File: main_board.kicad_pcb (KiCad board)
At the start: 2 copper layers, 142.2 x 86.4 mm, 4 parts, among them P1 CONN_02X04, U1 socket_leon_x3_dil64, U2 socket_pololu_24v12, U3 socket_pololu_24v12

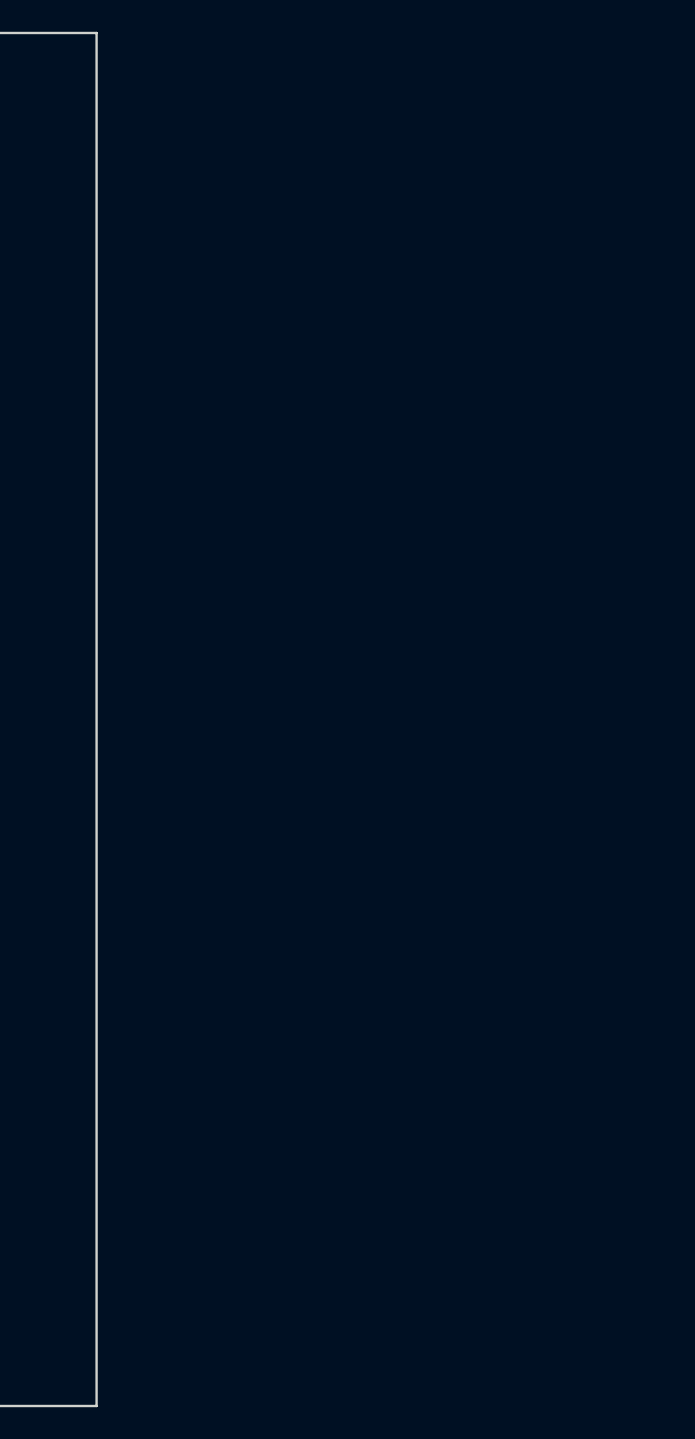
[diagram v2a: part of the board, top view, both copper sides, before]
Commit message: pcb: fix width size
Signed-off-by: Yannick Gicquel <ygicquel@gmail.com>
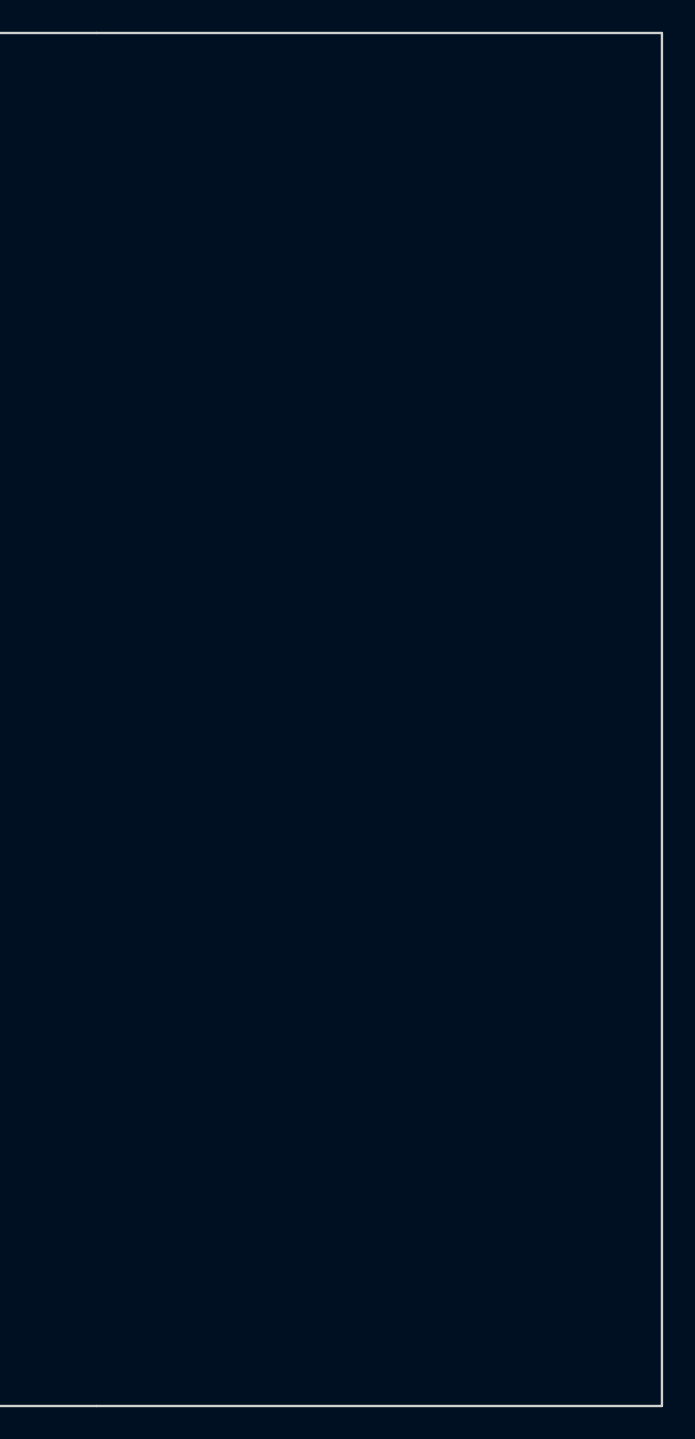
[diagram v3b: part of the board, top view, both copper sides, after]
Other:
- board size 142.2 x 86.4 mm -> 177.8 x 86.4 mm
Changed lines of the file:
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@@
     (links 27)
     (no_connects 25)
-    (area 35.484999 49.454999 177.875001 135.965001)
+    (area 35.484999 49.254999 177.875001 135.965001)
     (thickness 1.6)
-    (drawings 4)
+    (drawings 6)
     (tracks 6)
     (zones 0)
@@
     )
   )
-  (gr_line (start 177.8 49.53) (end 177.8 135.89) (angle 90) (layer Edge.Cuts) (width 0.15))
+  (gr_line (start 213.36 49.53) (end 177.8 49.53) (angle 90) (layer Edge.Cuts) (width 0.15))
+  (gr_line (start 213.36 135.89) (end 213.36 49.53) (angle 90) (layer Edge.Cuts) (width 0.15))
+  (gr_line (start 177.8 135.89) (end 213.36 135.89) (angle 90) (layer Edge.Cuts) (width 0.15))
   (gr_line (start 35.56 135.89) (end 35.56 49.53) (angle 90) (layer Edge.Cuts) (width 0.15))
   (gr_line (start 177.8 49.53) (end 35.56 49.53) (angle 90) (layer Edge.Cuts) (width 0.15))

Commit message: pcb: routing test and holes
Signed-off-by: Yannick Gicquel <ygicquel@gmail.com>
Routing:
- net ENC_B_L: track 0.00 -> 93.9 mm
- net PWM_R: track 0.00 -> 92.0 mm
- net ENC_A_L: track 0.00 -> 51.1 mm
- net DIR_L: track 0.00 -> 47.3 mm
- net DIR_R: track 0.00 -> 28.8 mm
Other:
- outline, holes or cut-outs redrawn
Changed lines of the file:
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@@
   (general
     (links 27)
-    (no_connects 25)
+    (no_connects 20)
     (area 35.484999 49.254999 177.875001 135.965001)
     (thickness 1.6)
-    (drawings 6)
-    (tracks 6)
+    (drawings 10)
+    (tracks 37)
     (zones 0)
     (modules 4)
@@
     )
   )
+  (gr_circle (center 39.37 53.34) (end 40.64 53.34) (layer Edge.Cuts) (width 0.15))
+  (gr_circle (center 209.55 53.34) (end 209.55 52.07) (layer Edge.Cuts) (width 0.15))
+  (gr_circle (center 209.55 132.08) (end 210.82 132.08) (layer Edge.Cuts) (width 0.15))
+  (gr_circle (center 39.37 132.08) (end 40.64 132.08) (layer Edge.Cuts) (width 0.15))
   (gr_line (start 213.36 49.53) (end 177.8 49.53) (angle 90) (layer Edge.Cuts) (width 0.15))
   (gr_line (start 213.36 135.89) (end 213.36 49.53) (angle 90) (layer Edge.Cuts) (width 0.15))
@@
   (gr_line (start 177.8 49.53) (end 35.56 49.53) (angle 90) (layer Edge.Cuts) (width 0.15))
   (gr_line (start 35.56 135.89) (end 177.8 135.89) (angle 90) (layer Edge.Cuts) (width 0.15))
+  (segment (start 74.93 105.41) (end 74.93 69.85) (width 0.25) (layer B.Cu) (net 63))
+  (segment (start 78.74 66.04) (end 85.09 66.04) (width 0.25) (layer B.Cu) (net 63))
+  (segment (start 74.93 69.85) (end 78.74 66.04) (width 0.25) (layer B.Cu) (net 63))
+  (segment (start 72.39 105.41) (end 72.39 106.68) (width 0.25) (layer B.Cu) (net 64))
+  (segment (start 78.74 91.44) (end 85.09 91.44) (width 0.25) (layer B.Cu) (net 64))
+  (segment (start 76.2 93.98) (end 78.74 91.44) (width 0.25) (layer B.Cu) (net 64))
+  (segment (start 76.2 106.68) (end 76.2 93.98) (width 0.25) (layer B.Cu) (net 64))
+  (segment (start 74.93 107.95) (end 76.2 106.68) (width 0.25) (layer B.Cu) (net 64))
+  (segment (start 73.66 107.95) (end 74.93 107.95) (width 0.25) (layer B.Cu) (net 64))
+  (segment (start 72.39 106.68) (end 73.66 107.95) (width 0.25) (layer B.Cu) (net 64))
+  (segment (start 77.47 128.27) (end 77.47 128.62) (width 0.25) (layer B.Cu) (net 65))
+  (segment (start 104.14 88.9) (end 85.09 88.9) (width 0.25) (layer B.Cu) (net 66))
+  (segment (start 106.68 91.44) (end 104.14 88.9) (width 0.25) (layer B.Cu) (net 66))
+  (segment (start 106.68 130.81) (end 106.68 91.44) (width 0.25) (layer B.Cu) (net 66))
+  (segment (start 84.74 133.35) (end 104.14 133.35) (width 0.25) (layer B.Cu) (net 66))
+  (segment (start 104.14 133.35) (end 106.68 130.81) (width 0.25) (layer B.Cu) (net 66))
+  (segment (start 80.01 128.27) (end 80.01 128.62) (width 0.25) (layer B.Cu) (net 66))
+  (segment (start 80.01 128.62) (end 84.74 133.35) (width 0.25) (layer B.Cu) (net 66))
+  (segment (start 43.18 116.84) (end 44.45 118.11) (width 0.25) (layer B.Cu) (net 67))
+  (segment (start 85.09 120.65) (end 85.09 128.27) (width 0.25) (layer B.Cu) (net 67))
+  (segment (start 82.55 118.11) (end 85.09 120.65) (width 0.25) (layer B.Cu) (net 67))
+  (segment (start 44.45 118.11) (end 82.55 118.11) (width 0.25) (layer B.Cu) (net 67))
+  (segment (start 104.14 121.92) (end 104.14 130.81) (width 0.25) (layer B.Cu) (net 68))
+  (segment (start 44.45 115.57) (end 99.06 115.57) (width 0.25) (layer B.Cu) (net 68))
+  (segment (start 99.06 115.57) (end 104.14 120.65) (width 0.25) (layer B.Cu) (net 68))
+  (segment (start 104.14 120.65) (end 104.14 121.92) (width 0.25) (layer B.Cu) (net 68))
+  (segment (start 43.18 114.3) (end 44.45 115.57) (width 0.25) (layer B.Cu) (net 68))
+  (segment (start 87.63 130.81) (end 87.63 128.27) (width 0.25) (layer B.Cu) (net 68))
+  (segment (start 88.9 132.08) (end 87.63 130.81) (width 0.25) (layer B.Cu) (net 68))
+  (segment (start 102.87 132.08) (end 88.9 132.08) (width 0.25) (layer B.Cu) (net 68))
+  (segment (start 104.14 130.81) (end 102.87 132.08) (width 0.25) (layer B.Cu) (net 68))
   (segment (start 102.87 128.27) (end 102.87 120.65) (width 0.25) (layer B.Cu) (net 69))
   (segment (start 99.06 116.84) (end 45.72 116.84) (width 0.25) (layer B.Cu) (net 69))

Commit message: all: add UARTC0 (debug link)
Signed-off-by: Yannick Gicquel <ygicquel@gmail.com>
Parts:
- added P2: CONN_01X05, Pin_Headers:Pin_Header_Straight_1x05, F.Cu at (128.3, 55.9)
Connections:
- U1 pad 18: Net-(U1-Pad18) -> UART0_TXD
- U1 pad 19: Net-(U1-Pad19) -> UART0_RXD

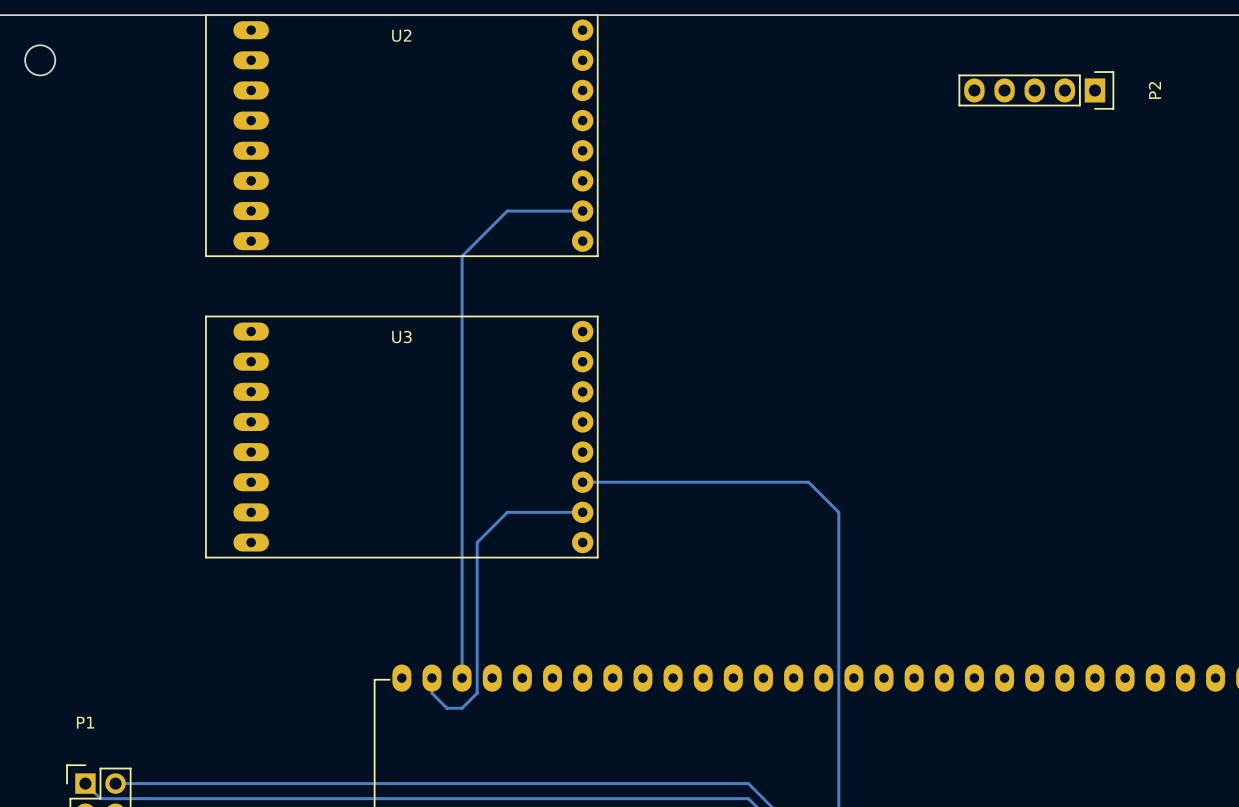
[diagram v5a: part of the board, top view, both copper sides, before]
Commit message: sch: move to hierarchical schematic and multiple sheets
Signed-off-by: Yannick Gicquel <ygicquel@gmail.com>
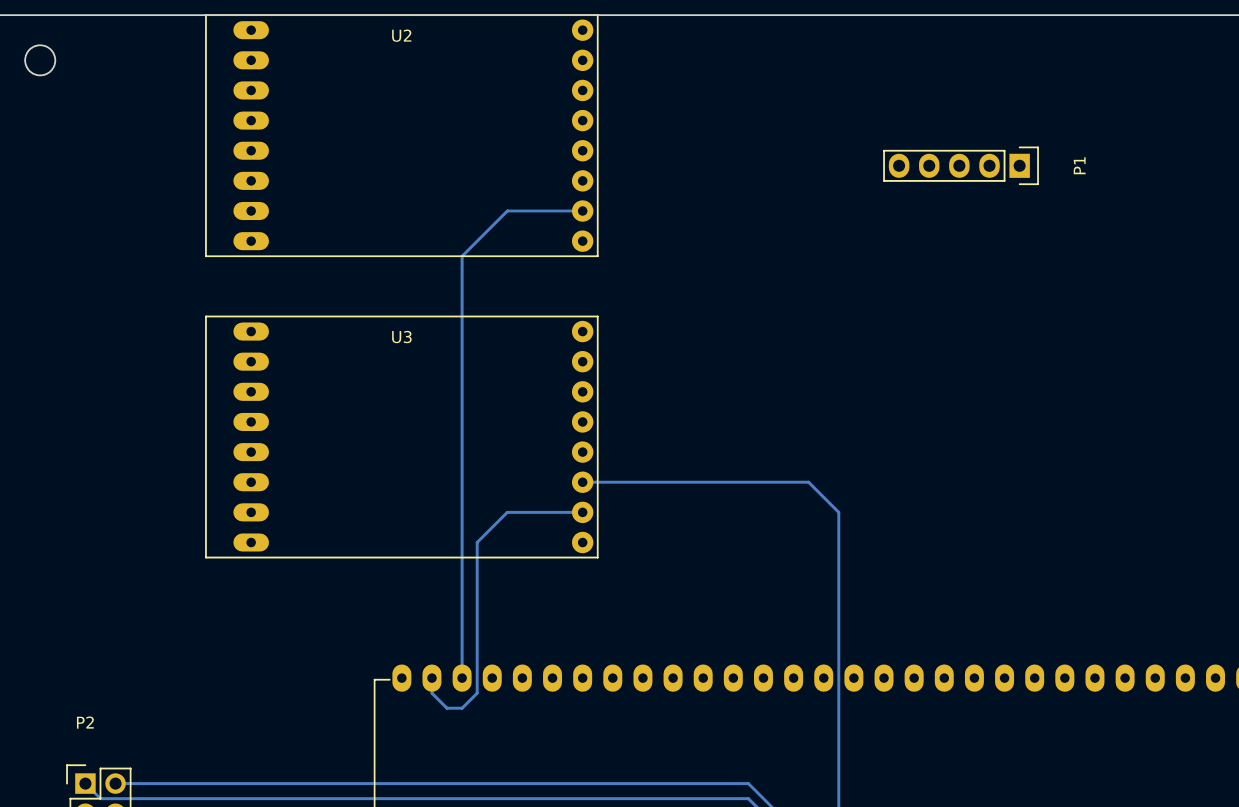
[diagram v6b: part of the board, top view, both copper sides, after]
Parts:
- P1: value CONN_02X04 -> CONN_01X05; footprint Pin_Headers:Pin_Header_Straight_2x04 -> Pin_Headers:Pin_Header_Straight_1x05
- P2: value CONN_01X05 -> CONN_02X04; footprint Pin_Headers:Pin_Header_Straight_1x05 -> Pin_Headers:Pin_Header_Straight_2x04
- moved P2 103.2 mm to (43.2, 114.3), turned to 0 degrees
- moved P1 94.4 mm to (121.9, 62.2), turned to 270 degrees
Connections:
- net DIR_L renamed /Sheet_MCU/DIR_L
- net DIR_R renamed /Sheet_MCU/DIR_R
- net OUTA_L renamed /Sheet_Motors/OUTA_L
- net OUTA_R renamed /Sheet_Motors/OUTA_R
- net OUTB_L renamed /Sheet_Motors/OUTB_L
- net OUTB_R renamed /Sheet_Motors/OUTB_R
- net PWM_L renamed /Sheet_MCU/PWM_L
- net PWM_R renamed /Sheet_MCU/PWM_R
- P1 pad 1: ENC_B_L -> Net-(P1-Pad1)
- P1 pad 2: ENC_B_R -> /Sheet_Connectors/UART_DBG_TXD
- P1 pad 3: ENC_A_L -> /Sheet_Connectors/UART_DBG_RXD
- P1 pad 4: ENC_A_R -> GND
- P1 pad 5: +3V3 -> Net-(P1-Pad5)
- P2 pad 1: Net-(P2-Pad1) -> ENCB_L
- P2 pad 2: UART0_TXD -> ENCB_R
- P2 pad 3: UART0_RXD -> ENCA_L
- P2 pad 4: GND -> ENCA_R
- P2 pad 5: Net-(P2-Pad5) -> +3V3
- U1 pad 18: UART0_TXD -> /Sheet_Connectors/UART_DBG_TXD
- U1 pad 19: UART0_RXD -> /Sheet_Connectors/UART_DBG_RXD
- U1 pad 39: ENC_A_L -> ENCA_L
- U1 pad 40: ENC_B_L -> ENCB_L
- U1 pad 46: ENC_A_R -> ENCA_R
- U1 pad 47: ENC_B_R -> ENCB_R
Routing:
- net ENC_B_L: track 93.9 -> 0.00 mm
- net ENCB_L: track 0.00 -> 93.9 mm
- net ENC_B_R: track 69.9 -> 0.00 mm
- net ENCB_R: track 0.00 -> 69.9 mm
- net ENC_A_R: track 66.3 -> 0.00 mm
- net ENCA_R: track 0.00 -> 66.3 mm
- net ENC_A_L: track 51.1 -> 0.00 mm
- net ENCA_L: track 0.00 -> 51.1 mm

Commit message: sch: add main_board_psu
subsheet contains PSU relevant parts

Signed-off-by: Yannick Gicquel <ygicquel@gmail.com>
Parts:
- added P3: CONN_01X02, Terminal_Blocks:TerminalBlock_Pheonix_MKDS1.5-2pol, F.Cu at (191.8, 57.1)
- added U4: socket_lm2596_mod, bot_parts:lm2596s_mod, F.Cu at (157.5, 68.6)
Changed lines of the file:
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@@
-(kicad_pcb (version 4) (host pcbnew 4.0.2+e4-6225~38~ubuntu15.10.1-stable)
+(kicad_pcb (version 4) (host pcbnew 4.0.4+e1-6308~48~ubuntu16.04.1-stable)
   (general
-    (links 30)
-    (no_connects 23)
+    (links 35)
+    (no_connects 28)
     (area 35.484999 49.454999 213.435001 135.965001)
     (thickness 1.6)
@@
     (tracks 37)
     (zones 0)
-    (modules 5)
-    (nets 80)
+    (modules 7)
+    (nets 81)
   )
   (page A4)
@@
   (net 78 /Sheet_Motors/OUTA_R)
   (net 79 /Sheet_Motors/OUTB_R)
+  (net 80 +5V)
   (net_class Default "This is the default net class."
     (clearance 0.2)
@@
     (add_net +24V)
     (add_net +3V3)
+    (add_net +5V)
     (add_net /Sheet_Connectors/UART_DBG_RXD)
     (add_net /Sheet_Connectors/UART_DBG_TXD)
@@
     )
   )
+  (module Terminal_Blocks:TerminalBlock_Pheonix_MKDS1.5-2pol (layer F.Cu)
+    (at 191.77 57.15)
+    (descr "2-way 5mm pitch terminal block, Phoenix MKDS series")
+    (fp_text reference P3 (at 2.5 5.9) (layer F.SilkS)
+      (effects (font (size 1 1) (thickness 0.15)))
+    )
+    (fp_text value CONN_01X02 (at 2.5 -6.6) (layer F.Fab)
+      (effects (font (size 1 1) (thickness 0.15)))
+    )
+    (fp_line (start -2.7 -5.4) (end 7.7 -5.4) (layer F.CrtYd) (width 0.05))
+    (fp_line (start -2.7 4.8) (end -2.7 -5.4) (layer F.CrtYd) (width 0.05))
+    (fp_line (start 7.7 4.8) (end -2.7 4.8) (layer F.CrtYd) (width 0.05))
+    (fp_line (start 7.7 -5.4) (end 7.7 4.8) (layer F.CrtYd) (width 0.05))
+    (fp_line (start 2.5 4.1) (end 2.5 4.6) (layer F.SilkS) (width 0.15))
+    (fp_circle (center 5 0.1) (end 3 0.1) (layer F.SilkS) (width 0.15))
+    (fp_circle (center 0 0.1) (end 2 0.1) (layer F.SilkS) (width 0.15))
+    (fp_line (start -2.5 2.6) (end 7.5 2.6) (layer F.SilkS) (width 0.15))
+    (fp_line (start -2.5 -2.3) (end 7.5 -2.3) (layer F.SilkS) (width 0.15))
+    (fp_line (start -2.5 4.1) (end 7.5 4.1) (layer F.SilkS) (width 0.15))
+    (fp_line (start -2.5 4.6) (end 7.5 4.6) (layer F.SilkS) (width 0.15))
+    (fp_line (start 7.5 4.6) (end 7.5 -5.2) (layer F.SilkS) (width 0.15))
+    (fp_line (start 7.5 -5.2) (end -2.5 -5.2) (layer F.SilkS) (width 0.15))
+    (fp_line (start -2.5 -5.2) (end -2.5 4.6) (layer F.SilkS) (width 0.15))
+    (pad 1 thru_hole rect (at 0 0) (size 2.5 2.5) (drill 1.3) (layers *.Cu *.Mask F.SilkS)
+      (net 62 GND))
+    (pad 2 thru_hole circle (at 5 0) (size 2.5 2.5) (drill 1.3) (layers *.Cu *.Mask F.SilkS)
+      (net 61 +24V))
+    (model Terminal_Blocks.3dshapes/TerminalBlock_Pheonix_MKDS1.5-2pol.wrl
+      (at (xyz 0.0984 0 0))
+      (scale (xyz 1 1 1))
+      (rotate (xyz 0 0 0))
+    )
+  )
+  (module bot_parts:lm2596s_mod (layer F.Cu)
+    (at 157.48 68.58 180)
+    (fp_text reference U4 (at 0 10.16 180) (layer F.SilkS)
+      (effects (font (size 1 1) (thickness 0.15)))
+    )
+    (fp_text value socket_lm2596_mod (at 0 -10.16 180) (layer F.Fab)
+      (effects (font (size 1 1) (thickness 0.15)))
+    )
+    (fp_line (start -22.86 -11.43) (end 22.86 -11.43) (layer F.SilkS) (width 0.15))
+    (fp_line (start 22.86 -11.43) (end 22.86 11.43) (layer F.SilkS) (width 0.15))
+    (fp_line (start 22.86 11.43) (end -22.86 11.43) (layer F.SilkS) (width 0.15))
+    (fp_line (start -22.86 11.43) (end -22.86 -11.43) (layer F.SilkS) (width 0.15))
+    (pad 1 thru_hole rect (at -19.05 -7.62 180) (size 4.5 4.5) (drill 1.5) (layers *.Cu *.Mask)
+      (net 61 +24V))
+    (pad 2 thru_hole rect (at -19.05 7.62 180) (size 4.5 4.5) (drill 1.5) (layers *.Cu *.Mask)
+      (net 62 GND))
+    (pad 3 thru_hole rect (at 19.05 -7.62 180) (size 4.5 4.5) (drill 1.5) (layers *.Cu *.Mask)
+      (net 80 +5V))
+    (pad 4 thru_hole rect (at 19.05 7.62 180) (size 4.5 4.5) (drill 1.5) (layers *.Cu *.Mask)
+      (net 62 GND))
+  )
   (gr_circle (center 39.37 53.34) (end 40.64 53.34) (layer Edge.Cuts) (width 0.15))
